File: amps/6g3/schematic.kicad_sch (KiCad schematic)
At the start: 79 parts, among them T1 125P2A, T2 125A1A

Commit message: Fix: schematic sheets — real title block, fitted paper, no lettering through circuitry
Every sheet in the corpus shipped with an EMPTY title block ("Title:" and
"Date:" blank, default "Sheet /" furniture) laid onto a fixed A4/A3 page
regardless of the drawing's size, with prose annotations placed by hand
wherever a coordinate looked free when the amp was first drawn. The result
read as an unfinished alpha under a `verified` badge: KiCanvas's default view
is `zoom_to_page()`, so a 150 x 110 mm circuit on an A3 sheet opened as a
postage stamp, and later edits had pushed live circuitry under the prose.

schematic_lib.py — the builder now records each element as a (kind, points,
extra) tuple instead of a finished string, so `write()` can measure and move
what it emits:

- emits a real `(title_block …)` read from the amp's own meta.yaml — Title =
  designation + style, Date = the verification (or added) date, Rev = the
  verification status, Company = Circuit Codex, plus the licence and source
  URL as comments. Fixes all 34 sheets from one place;
- emits `(paper "User" w h)` cut to the drawing, translated to a fixed margin,
  with the bottom 34 mm strip reserved for the worksheet's title block. Sheet
  utilisation of the drawable area went from as low as ~20% to 92-98%;
- `note()` queues prose into a wrapped band under the circuit, and `caption()`
  places a section heading over the block it names, nudging it clear if it
  would print through anything;
- per-symbol default label offsets (the old single default printed every pot's
  value through its own wiper arrow and every transformer's designator through
  its body), plus `place_labels()`, which moves any designator/value block that
  would print over ink;
- transformers and chokes are drawn, not boxed: iron core between two windings,
  centre taps where the part has them, and an optional `spec` lettering slot for
  a ratio or impedance;
- `gnd()` takes a direction, because a flag defaulting to "down" at the HEAD of
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
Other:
- note removed: "6G3 — Brown Deluxe-style · Circuit Codex · CC-BY-SA 4.0 · redrawn from circuit facts"
- company: (none) -> Circuit Codex
- title: (none) -> 6G3 — Brown Deluxe-style

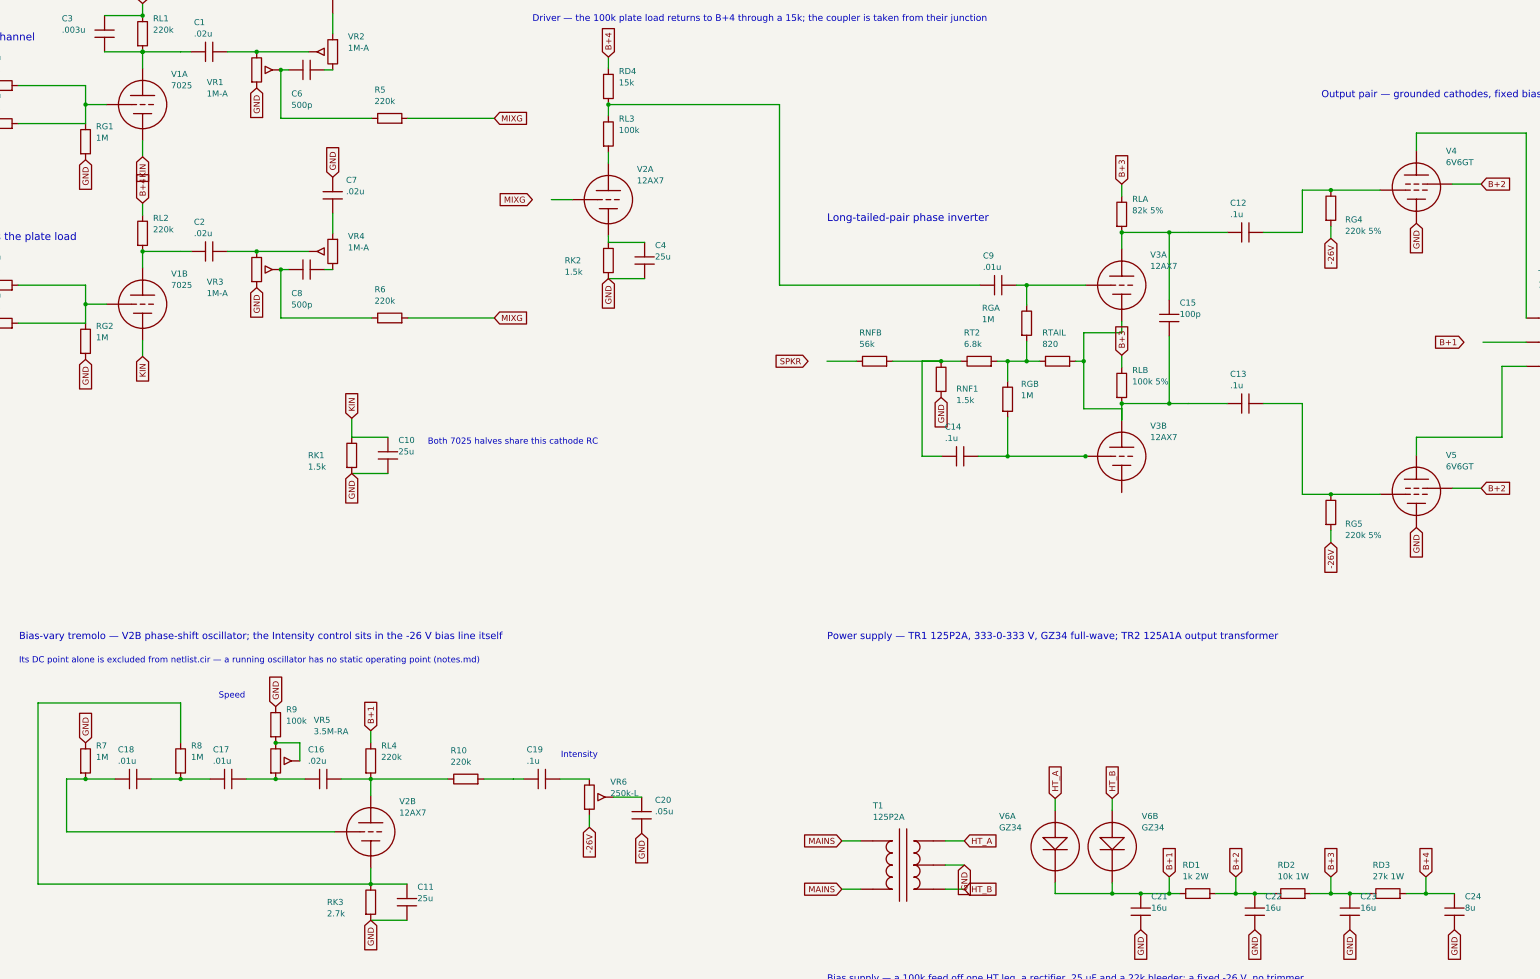
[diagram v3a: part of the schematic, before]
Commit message: Fix: deterministic schematic ids and wires split at every join
- _u() is uuid5 over (amp id, emission order), so a regeneration of an
  unchanged script is byte-identical and a drift gate becomes possible
- write() splits wire segments at symbol pins, wire ends and junction dots,
  so the file connects exactly what the drawing shows under KiCad's
  endpoint-only semantics (270 pins were on a wire's interior; net
  partitions unchanged on all 38 sheets)
- all sheets regenerated; aa864-bassman title block was stale (draft) and
  now matches meta.yaml (verified)

Co-Authored-By: Claude Fable 5.1 <noreply@anthropic.com>
Claude-Session: https://claude.ai/code/session_01KBMfdh37HmCL2iWcBiL5J1
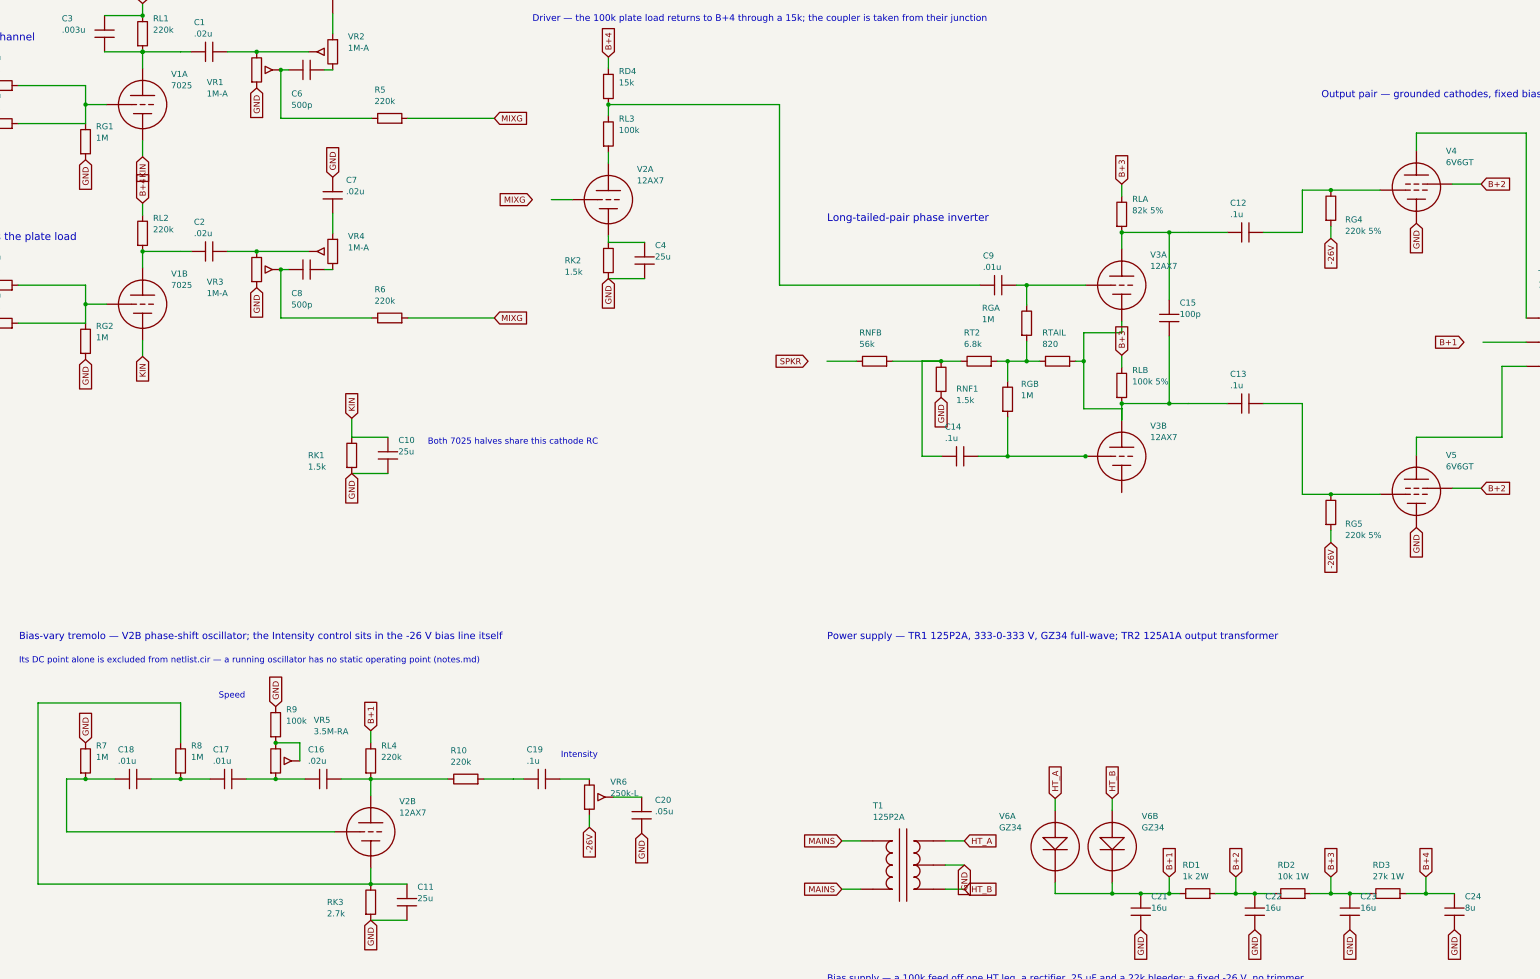
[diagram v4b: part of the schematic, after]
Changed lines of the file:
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@@
   (wire (pts (xy 60.51 47.738) (xy 74.7 47.738))
     (stroke (width 0) (type default)))
-  (wire (pts (xy 74.7 39.738) (xy 74.7 47.738))
+  (wire (pts (xy 74.7 39.738) (xy 74.7 43.738))
+    (stroke (width 0) (type default)))
+  (wire (pts (xy 74.7 43.738) (xy 74.7 47.738))
     (stroke (width 0) (type default)))
   (junction (at 74.7 43.738) (diameter 0) (color 0 0 0 0))
@@
   (wire (pts (xy 60.51 89.738) (xy 74.7 89.738))
     (stroke (width 0) (type default)))
-  (wire (pts (xy 74.7 81.738) (xy 74.7 89.738))
+  (wire (pts (xy 74.7 81.738) (xy 74.7 85.738))
+    (stroke (width 0) (type default)))
+  (wire (pts (xy 74.7 85.738) (xy 74.7 89.738))
     (stroke (width 0) (type default)))
   (junction (at 74.7 85.738) (diameter 0) (color 0 0 0 0))
@@
   (wire (pts (xy 220.7 81.738) (xy 262.89 81.738))
     (stroke (width 0) (type default)))
-  (wire (pts (xy 270.51 81.738) (xy 285.08 81.738))
+  (wire (pts (xy 270.51 81.738) (xy 272.7 81.738))
+    (stroke (width 0) (type default)))
+  (wire (pts (xy 272.7 81.738) (xy 285.08 81.738))
     (stroke (width 0) (type default)))
   (symbol (lib_id "cx:TRIODE") (at 292.7 81.738 0) (unit 1)
@@
   (global_label "B+3" (shape input) (at 292.7 60.478 90)
     (effects (font (size 1.27 1.27)) (justify left)))
-  (wire (pts (xy 292.7 110.118) (xy 292.7 106.638))
+  (wire (pts (xy 292.7 110.118) (xy 292.7 107.738))
+    (stroke (width 0) (type default)))
+  (wire (pts (xy 292.7 107.738) (xy 292.7 106.638))
     (stroke (width 0) (type default)))
   (symbol (lib_id "cx:R") (at 292.7 102.828 0) (unit 1)
@@
   (wire (pts (xy 292.7 107.738) (xy 284.7 107.738))
     (stroke (width 0) (type default)))
-  (wire (pts (xy 284.7 91.738) (xy 284.7 107.738))
+  (wire (pts (xy 284.7 91.738) (xy 284.7 97.738))
+    (stroke (width 0) (type default)))
+  (wire (pts (xy 284.7 97.738) (xy 284.7 107.738))
     (stroke (width 0) (type default)))
   (junction (at 284.7 97.738) (diameter 0) (color 0 0 0 0))
@@
     (property "Reference" "RT2" (at 259.5 91.738 270) (effects (font (size 1.27 1.27)) (justify left)))
     (property "Value" "6.8k" (at 259.5 94.138 270) (effects (font (size 1.27 1.27)) (justify left))))
-  (wire (pts (xy 266.51 97.738) (xy 272.7 97.738))
+  (wire (pts (xy 266.51 97.738) (xy 268.7 97.738))
+    (stroke (width 0) (type default)))
+  (wire (pts (xy 268.7 97.738) (xy 272.7 97.738))
     (stroke (width 0) (type default)))
   (wire (pts (xy 258.89 97.738) (xy 254.7 97.738))
@@
     (property "Reference" "RNFB" (at 237.5 91.738 270) (effects (font (size 1.27 1.27)) (justify left)))
     (property "Value" "56k" (at 237.5 94.138 270) (effects (font (size 1.27 1.27)) (justify left))))
-  (wire (pts (xy 244.51 97.738) (xy 254.7 97.738))
+  (wire (pts (xy 244.51 97.738) (xy 250.7 97.738))
+    (stroke (width 0) (type default)))
+  (wire (pts (xy 250.7 97.738) (xy 254.7 97.738))
     (stroke (width 0) (type default)))
   (wire (pts (xy 230.7 97.738) (xy 236.89 97.738))
@@
     (stroke (width 0) (type default)))
   (junction (at 292.7 70.638) (diameter 0) (color 0 0 0 0))
-  (wire (pts (xy 292.7 70.638) (xy 306.7 70.638))
+  (wire (pts (xy 292.7 70.638) (xy 302.7 70.638))
+    (stroke (width 0) (type default)))
+  (wire (pts (xy 302.7 70.638) (xy 306.7 70.638))
     (stroke (width 0) (type default)))
   (junction (at 292.7 106.638) (diameter 0) (color 0 0 0 0))
-  (wire (pts (xy 292.7 106.638) (xy 306.7 106.638))
+  (wire (pts (xy 292.7 106.638) (xy 302.7 106.638))
+    (stroke (width 0) (type default)))
+  (wire (pts (xy 302.7 106.638) (xy 306.7 106.638))
     (stroke (width 0) (type default)))
   (junction (at 302.7 70.638) (diameter 0) (color 0 0 0 0))
@@
   (text "Output pair — grounded cathodes, fixed bias" (at 334.7 41.738 0)
     (effects (font (size 1.5 1.5)) (justify left)))
-  (wire (pts (xy 330.7 61.738) (xy 347.08 61.738))
+  (wire (pts (xy 330.7 61.738) (xy 336.7 61.738))
+    (stroke (width 0) (type default)))
+  (wire (pts (xy 336.7 61.738) (xy 347.08 61.738))
     (stroke (width 0) (type default)))
   (symbol (lib_id "cx:PENTODE") (at 354.7 61.103 0) (unit 1)
@@
   (global_label "GND" (shape input) (at 354.7 68.723 270)
     (effects (font (size 1.27 1.27)) (justify right)))
-  (wire (pts (xy 330.7 125.738) (xy 347.08 125.738))
+  (wire (pts (xy 330.7 125.738) (xy 336.7 125.738))
+    (stroke (width 0) (type default)))
+  (wire (pts (xy 336.7 125.738) (xy 347.08 125.738))
     (stroke (width 0) (type default)))
   (symbol (lib_id "cx:PENTODE") (at 354.7 125.103 0) (unit 1)
@@
   (wire (pts (xy 290.7 207.478) (xy 290.7 209.738))
     (stroke (width 0) (type default)))
-  (wire (pts (xy 278.7 209.738) (xy 302.7 209.738))
+  (wire (pts (xy 278.7 209.738) (xy 290.7 209.738))
+    (stroke (width 0) (type default)))
+  (wire (pts (xy 290.7 209.738) (xy 296.7 209.738))
+    (stroke (width 0) (type default)))
+  (wire (pts (xy 296.7 209.738) (xy 302.7 209.738))
     (stroke (width 0) (type default)))
   (junction (at 290.7 209.738) (diameter 0) (color 0 0 0 0))
@@
   (wire (pts (xy 302.7 209.738) (xy 304.89 209.738))
     (stroke (width 0) (type default)))
-  (wire (pts (xy 312.51 209.738) (xy 322.7 209.738))
+  (wire (pts (xy 312.51 209.738) (xy 316.7 209.738))
+    (stroke (width 0) (type default)))
+  (wire (pts (xy 316.7 209.738) (xy 320.7 209.738))
+    (stroke (width 0) (type default)))
+  (wire (pts (xy 320.7 209.738) (xy 322.7 209.738))
     (stroke (width 0) (type default)))
   (junction (at 316.7 209.738) (diameter 0) (color 0 0 0 0))
@@
   (wire (pts (xy 322.7 209.738) (xy 324.89 209.738))
     (stroke (width 0) (type default)))
-  (wire (pts (xy 332.51 209.738) (xy 342.7 209.738))
+  (wire (pts (xy 332.51 209.738) (xy 336.7 209.738))
+    (stroke (width 0) (type default)))
+  (wire (pts (xy 336.7 209.738) (xy 340.7 209.738))
+    (stroke (width 0) (type default)))
+  (wire (pts (xy 340.7 209.738) (xy 342.7 209.738))
     (stroke (width 0) (type default)))
   (junction (at 336.7 209.738) (diameter 0) (color 0 0 0 0))
@@
   (wire (pts (xy 342.7 209.738) (xy 344.89 209.738))
     (stroke (width 0) (type default)))
-  (wire (pts (xy 352.51 209.738) (xy 362.7 209.738))
+  (wire (pts (xy 352.51 209.738) (xy 356.7 209.738))
+    (stroke (width 0) (type default)))
+  (wire (pts (xy 356.7 209.738) (xy 362.7 209.738))
     (stroke (width 0) (type default)))
   (junction (at 356.7 209.738) (diameter 0) (color 0 0 0 0))

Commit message: Fix: schematic wiring on 6g3, 6g4, 6g5, 6g6b
- long-tailed pair tail moved off section B's plate to its cathode (6g3,
  6g4, 6g5); 6g4 V8 plate lead was drawn under its grounded cathode
- 6g6b: all five OT leads on bare coordinates with the secondary drawn on
  the primary side; bias line taken off the bleeder's grounded end (NBIAS
  and GND one net); both tone networks rebuilt; mixing bus ran through
  V3A's bottle
- eight parts shorted end to end, invisible to the pin check: 6g4 RGL1;
  6g5 RG5 (mixing node on ground); 6g6b C11, RG4B, RNFB, RTAIL, RTN1, VR3
- 6g5: treble pot runs off each other's lug, driver run 12 mm short of
  V6A grid, CFB1 rotated but wired upright, choke leads short both ends
- five dated waivers (bridge rectifier centre tap, footswitch terminal
  not lettered on the source, mains side outside the drawing, VR7's
  undesignated cap)
- OPEN, not guessed: 6g5 presence network is drawn as a DC path to ground
  (RPRES + pot in series) while netlist.cir has RT2 to ground and calls the
  network DC-neutral; sources do not settle it — sheet stays unclaimed

Co-Authored-By: Claude Fable 5.1 <noreply@anthropic.com>
Claude-Session: https://claude.ai/code/session_01KBMfdh37HmCL2iWcBiL5J1
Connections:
- net B+1: now also T2.2 (CT)
- net BRIGHT 1: now also R3n.1
- net BRIGHT 2: now also R4n.1
- net HT_B: now also R11.1
- net MIXG: now also V2A.2 (G)
- net NORM 1: now also R1n.1
- net NORM 2: now also R2n.1
- net SPKR: now also RNFB.1
- net at C13.1, C15.2, RLB.2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: no longer RTAIL.2, V3A.3 (K)
- net at V3B.3 (K): now also RTAIL.2, V3A.3 (K)
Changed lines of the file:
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@@
     (property "Reference" "R1n" (at 53.5 33.738 270) (effects (font (size 1.27 1.27)) (justify left)))
     (property "Value" "68k" (at 53.5 36.138 270) (effects (font (size 1.27 1.27)) (justify left))))
-  (wire (pts (xy 50.7 39.738) (xy 52.89 39.738))
+  (wire (pts (xy 46.7 39.738) (xy 52.89 39.738))
     (stroke (width 0) (type default)))
   (wire (pts (xy 60.51 39.738) (xy 74.7 39.738))
@@
     (property "Reference" "R2n" (at 53.5 41.738 270) (effects (font (size 1.27 1.27)) (justify left)))
     (property "Value" "68k" (at 53.5 44.138 270) (effects (font (size 1.27 1.27)) (justify left))))
-  (wire (pts (xy 50.7 47.738) (xy 52.89 47.738))
+  (wire (pts (xy 46.7 47.738) (xy 52.89 47.738))
     (stroke (width 0) (type default)))
   (wire (pts (xy 60.51 47.738) (xy 74.7 47.738))
@@
     (property "Reference" "R3n" (at 53.5 75.738 270) (effects (font (size 1.27 1.27)) (justify left)))
     (property "Value" "68k" (at 53.5 78.138 270) (effects (font (size 1.27 1.27)) (justify left))))
-  (wire (pts (xy 50.7 81.738) (xy 52.89 81.738))
+  (wire (pts (xy 46.7 81.738) (xy 52.89 81.738))
     (stroke (width 0) (type default)))
   (wire (pts (xy 60.51 81.738) (xy 74.7 81.738))
@@
     (property "Reference" "R4n" (at 53.5 83.738 270) (effects (font (size 1.27 1.27)) (justify left)))
     (property "Value" "68k" (at 53.5 86.138 270) (effects (font (size 1.27 1.27)) (justify left))))
-  (wire (pts (xy 50.7 89.738) (xy 52.89 89.738))
+  (wire (pts (xy 46.7 89.738) (xy 52.89 89.738))
     (stroke (width 0) (type default)))
   (wire (pts (xy 60.51 89.738) (xy 74.7 89.738))
@@
     (property "Reference" "V2A" (at 190.7 57.338 0) (effects (font (size 1.27 1.27)) (justify left)))
     (property "Value" "12AX7" (at 190.7 59.738 0) (effects (font (size 1.27 1.27)) (justify left))))
-  (wire (pts (xy 172.7 63.738) (xy 177.08 63.738))
+  (wire (pts (xy 168.7 63.738) (xy 177.08 63.738))
     (stroke (width 0) (type default)))
   (wire (pts (xy 184.7 56.118) (xy 184.7 53.738))
@@
   (global_label "B+3" (shape input) (at 292.7 60.478 90)
     (effects (font (size 1.27 1.27)) (justify left)))
-  (wire (pts (xy 292.7 110.118) (xy 292.7 107.738))
-    (stroke (width 0) (type default)))
-  (wire (pts (xy 292.7 107.738) (xy 292.7 106.638))
+  (wire (pts (xy 292.7 110.118) (xy 292.7 106.638))
     (stroke (width 0) (type default)))
   (symbol (lib_id "cx:R") (at 292.7 102.828 0) (unit 1)
@@
   (wire (pts (xy 292.7 91.738) (xy 284.7 91.738))
     (stroke (width 0) (type default)))
-  (wire (pts (xy 292.7 110.118) (xy 292.7 107.738))
-    (stroke (width 0) (type default)))
-  (wire (pts (xy 292.7 107.738) (xy 284.7 107.738))
+  (wire (pts (xy 292.7 125.358) (xy 278.7 125.358))
+    (stroke (width 0) (type default)))
+  (wire (pts (xy 278.7 125.358) (xy 278.7 107.738))
+    (stroke (width 0) (type default)))
+  (wire (pts (xy 278.7 107.738) (xy 284.7 107.738))
     (stroke (width 0) (type default)))
   (wire (pts (xy 284.7 91.738) (xy 284.7 97.738))
@@
   (wire (pts (xy 250.7 97.738) (xy 254.7 97.738))
     (stroke (width 0) (type default)))
-  (wire (pts (xy 230.7 97.738) (xy 236.89 97.738))
+  (wire (pts (xy 226.7 97.738) (xy 236.89 97.738))
     (stroke (width 0) (type default)))
   (global_label "SPKR" (shape input) (at 226.7 97.738 180)
@@
   (wire (pts (xy 372.7 98.818) (xy 377.81 98.818))
     (stroke (width 0) (type default)))
-  (wire (pts (xy 377.81 93.738) (xy 368.7 93.738))
+  (wire (pts (xy 377.81 93.738) (xy 364.7 93.738))
     (stroke (width 0) (type default)))
   (global_label "B+1" (shape input) (at 364.7 93.738 180)
@@
     (property "Reference" "R11" (at 241.5 229.738 270) (effects (font (size 1.27 1.27)) (justify left)))
     (property "Value" "100k 5%" (at 241.5 232.138 270) (effects (font (size 1.27 1.27)) (justify left))))
-  (wire (pts (xy 234.7 235.738) (xy 240.89 235.738))
+  (wire (pts (xy 230.7 235.738) (xy 240.89 235.738))
     (stroke (width 0) (type default)))
   (wire (pts (xy 248.51 235.738) (xy 254.62 235.738))
